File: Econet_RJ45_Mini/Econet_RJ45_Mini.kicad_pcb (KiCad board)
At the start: 2 copper layers, 32.6 x 34 mm, 5 parts, among them J1 RJ45, J2 RJ45, J3 DIN-5_180degree

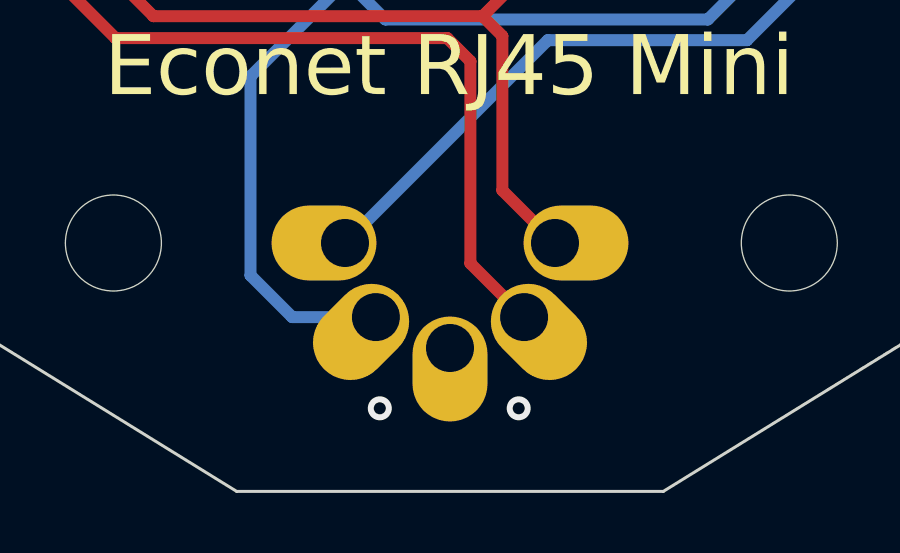
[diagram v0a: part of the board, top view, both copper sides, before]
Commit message: Make DIN connector bigger to increase tolerances
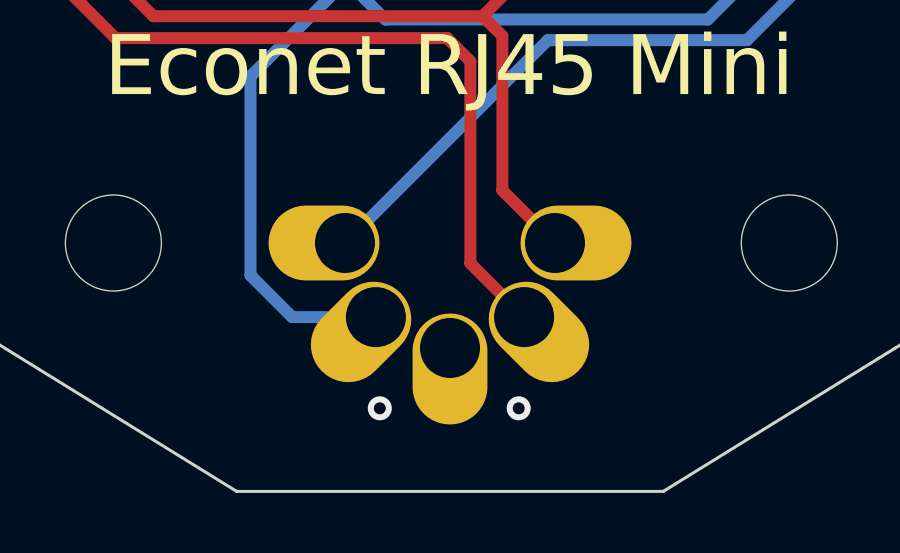
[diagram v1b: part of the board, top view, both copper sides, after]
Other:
- board text added: "v0.2"
- board text removed: "v0.1"
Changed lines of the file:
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@@
+      (effects (font (size 1 1) (thickness 0.15)) (justify mirror))
+    )
+    (fp_text user "Connector this side" (at 0.01 -3.49 180 unlocked) (layer "B.Fab")
       (effects (font (size 1 1) (thickness 0.15)) (justify mirror))
     )
     (fp_text user "${REFERENCE}" (at 0.26 -10.06 180 unlocked) (layer "B.Fab")
-      (effects (font (size 1 1) (thickness 0.15)) (justify mirror))
-    )
-    (fp_text user "Connector this side" (at 0.01 -3.49 180 unlocked) (layer "B.Fab")
       (effects (font (size 1 1) (thickness 0.15)) (justify mirror))
     )
@@
     (fp_circle (center 0 0) (end 7.15 0) (layer "B.CrtYd") (width 0.12) (fill none))
     (fp_circle (center 0 0) (end 7.15 0) (layer "F.CrtYd") (width 0.12) (fill none))
-    (pad "1" thru_hole oval (at 3.5 0) (size 3.5 2.5) (drill 1.6 (offset 0.7 0)) (layers *.Cu *.Mask)
+    (pad "1" thru_hole oval (at 3.5 0) (size 3.7 2.5) (drill 2 (offset 0.7 0)) (layers *.Cu *.Mask)
       (net 7 "/DATA+") (pintype "passive"))
-    (pad "2" thru_hole oval (at 0 3.5 270) (size 3.5 2.5) (drill 1.6 (offset 0.7 0)) (layers *.Cu *.Mask)
+    (pad "2" thru_hole oval (at 0 3.5 270) (size 3.7 2.5) (drill 2 (offset 0.7 0)) (layers *.Cu *.Mask)
       (net 4 "/GND") (pintype "passive"))
-    (pad "3" thru_hole oval (at -3.5 0 180) (size 3.5 2.5) (drill 1.6 (offset 0.7 0)) (layers *.Cu *.Mask)
+    (pad "3" thru_hole oval (at -3.5 0 180) (size 3.7 2.5) (drill 2 (offset 0.7 0)) (layers *.Cu *.Mask)
       (net 1 "/CLK-") (pintype "passive"))
-    (pad "4" thru_hole oval (at 2.47 2.47 315) (size 3.5 2.5) (drill 1.6 (offset 0.7 0)) (layers *.Cu *.Mask)
+    (pad "4" thru_hole oval (at 2.47 2.47 315) (size 3.7 2.5) (drill 2 (offset 0.7 0)) (layers *.Cu *.Mask)
       (net 6 "/DATA-") (pintype "passive"))
-    (pad "5" thru_hole oval (at -2.47 2.47 225) (size 3.5 2.5) (drill 1.6 (offset 0.7 0)) (layers *.Cu *.Mask)
+    (pad "5" thru_hole oval (at -2.47 2.47 225) (size 3.7 2.5) (drill 2 (offset 0.7 0)) (layers *.Cu *.Mask)
       (net 2 "/CLK+") (pintype "passive"))
   )
@@
     (effects (font (size 1.5 1.5) (thickness 0.3)) (justify mirror))
   )
-  (gr_text "v0.1" (at 165.95 50.54) (layer "B.SilkS")
+  (gr_text "v0.2" (at 165.95 50.54) (layer "B.SilkS")
     (effects (font (size 1.5 1.5) (thickness 0.3)) (justify mirror))
   )
